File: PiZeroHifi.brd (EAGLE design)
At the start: 65.3 x 30.1 mm, 43 parts, among them CON1 RPI-ZEROPI-ZERO-THRUHOLE, CON3 Audio Out, J1 GROVEGROVE-HORIZONTAL, J2 GROVEGROVE-HORIZONTAL, J3 GROVEGROVE-HORIZONTAL, U1 TXS0102, U2 LSM6DS33, U3 TC1014-3.3V, U4 PCM5101A, U5 PAM8403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

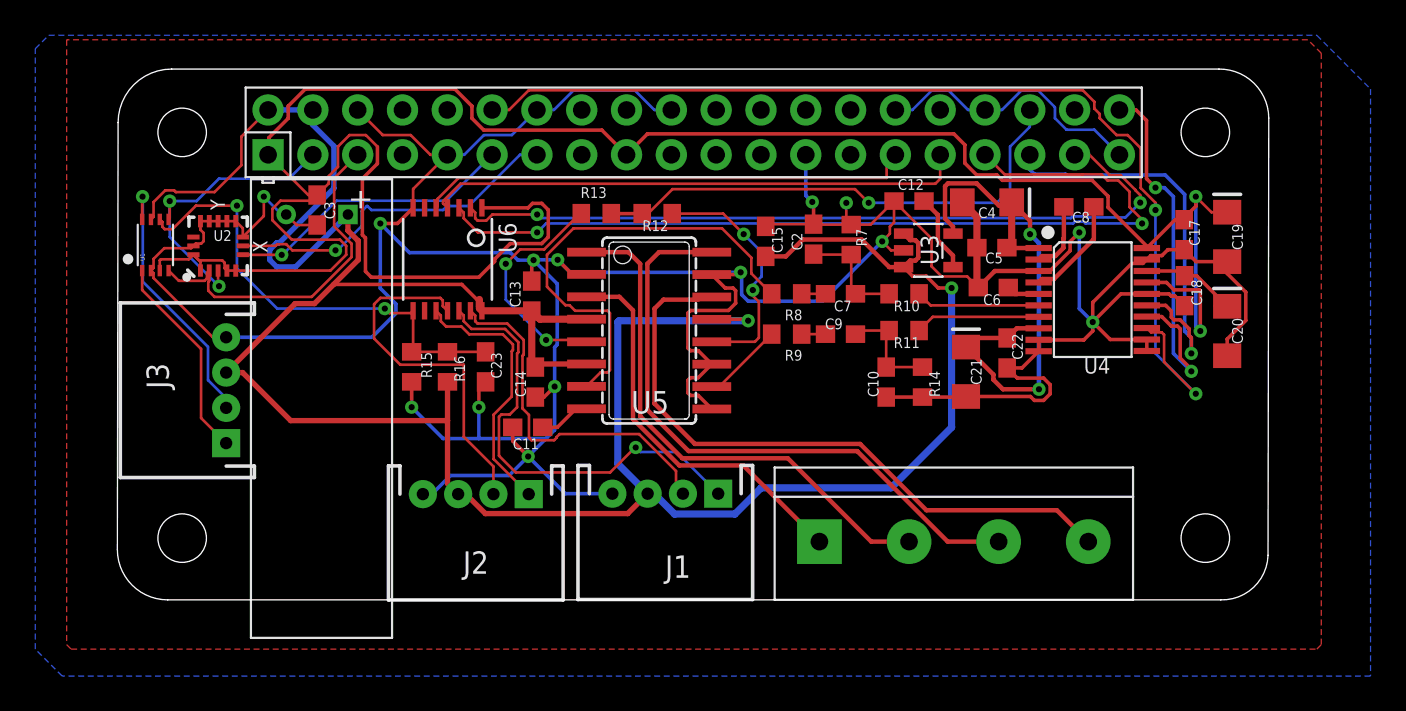
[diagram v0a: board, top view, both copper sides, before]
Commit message: Change position of GPIO
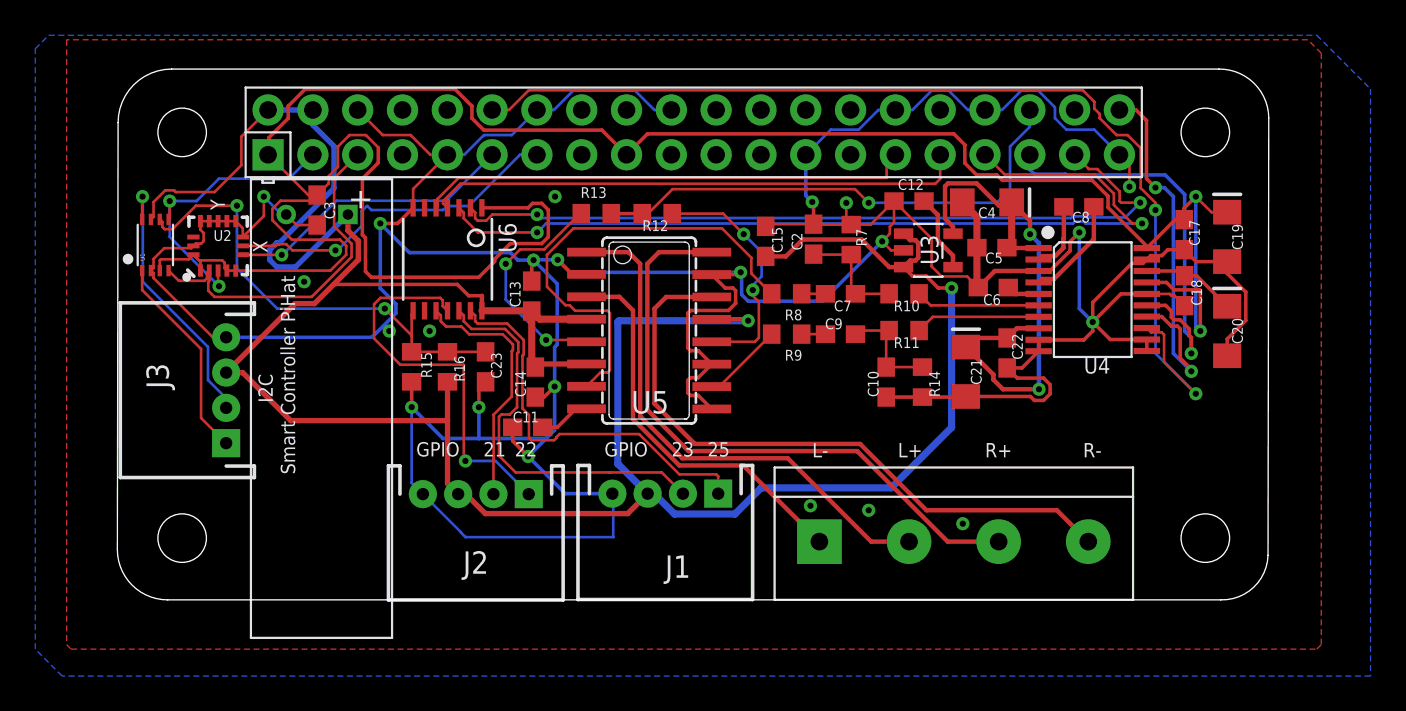
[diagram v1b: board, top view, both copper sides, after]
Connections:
- net GPI022-OUT: now also J2.1; no longer J2.2
- net GPIO21-OUT: now also J2.2; no longer J2.1
- net GPIO23-OUT: now also J1.2; no longer J1.1
- net GPIO25-OUT: now also J1.1; no longer J1.2
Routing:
- net GND: track 260.4 -> 281.1 mm, vias 14 -> 22
- net GPIO23-OUT: track 26.0 -> 22.8 mm, vias 1 -> 0
- net GPIO25-OUT: track 20.5 -> 22.5 mm
- net GPI022-OUT: track 20.5 -> 22.3 mm, vias 0 -> 1
- net GPIO21-OUT: track 15.1 -> 14.3 mm
- net +R: track 35.9 -> 35.2 mm
- net N$4: track 6.06 -> 5.38 mm
- net +5V: track 159.7 -> 159.1 mm
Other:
- board text added: "21"
- board text added: "22"
- board text added: "23"
- board text added: "25"
- board text added: "GPIO"
- board text added: "I2C"
- board text added: "L+"
- board text added: "L-"
- board text added: "R+"
- board text added: "R-"
- board text added: "Smart Controller PiHat"
